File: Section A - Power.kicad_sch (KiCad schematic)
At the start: 17 parts, among them J1 Screw_Terminal_01x02, Q6 IRFR5305, U1 XL1509-5.0, U2 LM1117MP-3.3

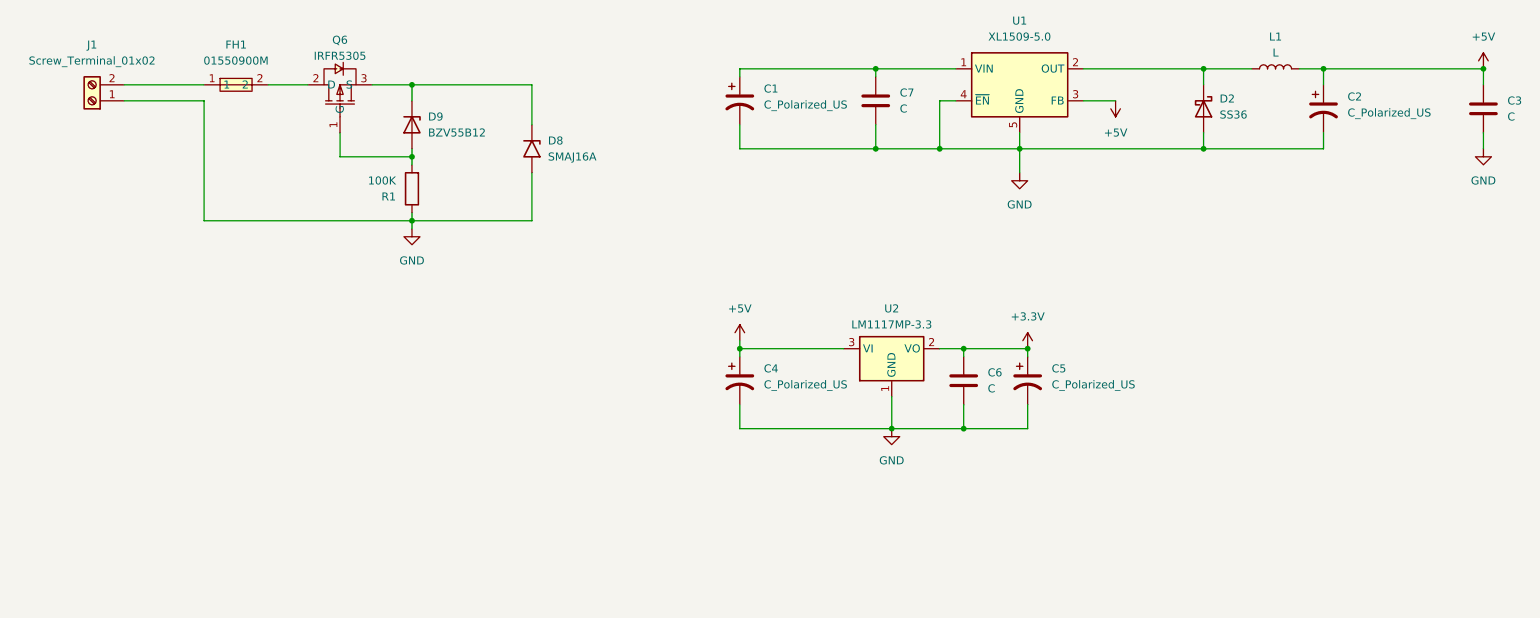
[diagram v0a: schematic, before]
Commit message: add CAN port, change power regulation
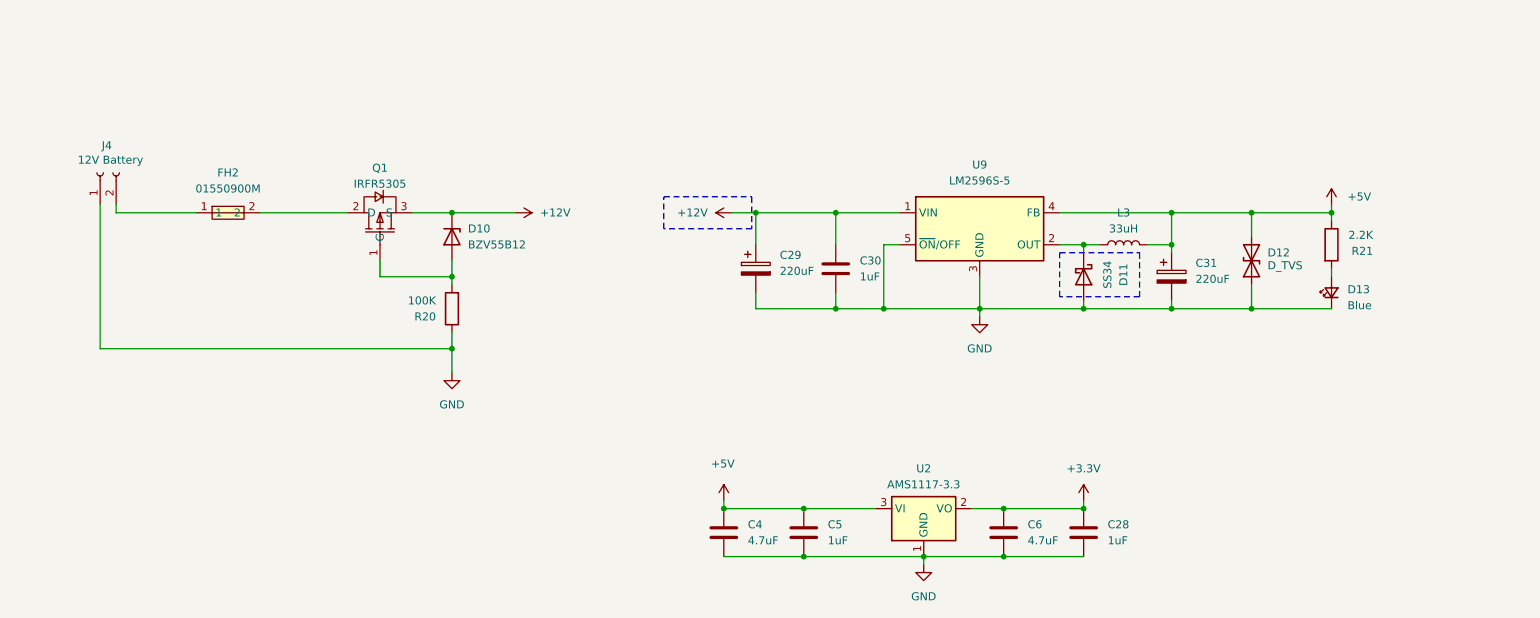
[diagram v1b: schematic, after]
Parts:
- removed C1, C2, C4, C5: C_Polarized_US, symbol Device:C_Polarized_US
- removed C3, C7: C, symbol Device:C
- removed D2: SS36, Diode_SMD:D_SMA, symbol Diode:SS36
- removed D8: SMAJ16A, Diode_SMD:D_SMA, symbol Diode:SMAJ16A
- removed D9: BZV55B12, Diode_SMD:D_MiniMELF, symbol Diode:BZV55B12
- removed FH1: 01550900M, easyeda2kicad:FUSE-SMD_L9.8-W5.0_01550900M, symbol easyeda2kicad:01550900M
- removed J1: Screw_Terminal_01x02, symbol Connector:Screw_Terminal_01x02
- removed L1: L, symbol Device:L
- removed Q6: IRFR5305, easyeda2kicad:TO-252-3_L6.6-W6.1-P4.58-LS10.1-BR-1, symbol easyeda2kicad:IRFR5305_C5155388
- removed R1: 100K, PCM_SparkFun-Resistor:R_0805_2012Metric, symbol Device:R
- removed U1: XL1509-5.0, Package_SO:SOIC-8_3.9x4.9mm_P1.27mm, symbol Regulator_Switching:XL1509-5.0
- removed U2: LM1117MP-3.3, Package_TO_SOT_SMD:SOT-223-3_TabPin2, symbol Regulator_Linear:LM1117MP-3.3
- added C28, C30, C5: 1uF, Capacitor_SMD:C_0805_2012Metric, symbol Device:C
- added C29, C31: 220uF, Capacitor_SMD:CP_Elec_8x10.5, symbol Device:C_Polarized
- added C4: 4.7uF, Capacitor_SMD:C_1206_3216Metric, symbol Device:C
- added D10: BZV55B12, Diode_SMD:D_MiniMELF, symbol Diode:BZV55B12
- added D11: SS34, easyeda2kicad:SMA_L4.4-W2.8-LS5.4-R-RD, symbol Device:D_Schottky
- added D12: D_TVS, Diode_SMD:D_SMA, symbol Device:D_TVS
- added D13: Blue, LED_SMD:LED_0805_2012Metric, symbol PCM_SparkFun-LED:LED_Blue_0603
- added FH2: 01550900M, easyeda2kicad:FUSE-SMD_L9.8-W5.0_01550900M, symbol easyeda2kicad:01550900M
- added J4: 12V Battery, TerminalBlock_Phoenix:TerminalBlock_Phoenix_MKDS-3-2-5.08_1x02_P5.08mm_Horizontal, symbol Connector:Conn_01x02_Socket
- added L3: 33uH, DR74-330-R:INDM7676X435N, symbol Device:L
- added Q1: IRFR5305, easyeda2kicad:TO-252-3_L6.6-W6.1-P4.58-LS10.1-BR-1, symbol easyeda2kicad:IRFR5305_C5155388
- added R20: 100K, Resistor_SMD:R_0805_2012Metric, symbol Device:R
- added R21: 2.2K, Resistor_SMD:R_0805_2012Metric, symbol Device:R
- added U2: AMS1117-3.3, Package_TO_SOT_SMD:SOT-223-3_TabPin2, symbol Regulator_Linear:AMS1117-3.3
- added U9: LM2596S-5, Package_TO_SOT_SMD:TO-263-5_TabPin3, symbol Regulator_Switching:LM2596S-5
- C6: value C -> 4.7uF; footprint (none) -> Capacitor_SMD:C_1206_3216Metric
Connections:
- net +3.3V: now also C28.1, U2.2 (VO)
- net +5V: now also C31.1, C4.1, C5.1, D12.2 (A2), L3.2, R21.1, U2.3 (VI), U9.4 (FB)
- net GND: now also C28.2, C29.2, C30.2, C31.2, C4.2, C5.2, D11.2 (A), D12.1 (A1), D13.1 (K), J4.1 (Pin_1), R20.1, U2.1 (GND), U9.3 (GND), U9.5 (~{ON}/OFF)
- new net: D11.1 (K), L3.1, U9.2 (OUT)
- new net: D10.2 (A), Q1.1 (G), R20.2
- new net: FH2.2, Q1.2 (D)
- new net: FH2.1, J4.2 (Pin_2)
- new net: D13.2 (A), R21.2
- new net +12V: C29.1, C30.1, D10.1 (K), Q1.3 (S), U9.1 (VIN)
